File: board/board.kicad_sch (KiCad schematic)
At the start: 8 parts, among them J1 015_RGMII, J2 020_1000BASE-T_with_CT, J3 Conn_01x03_Male

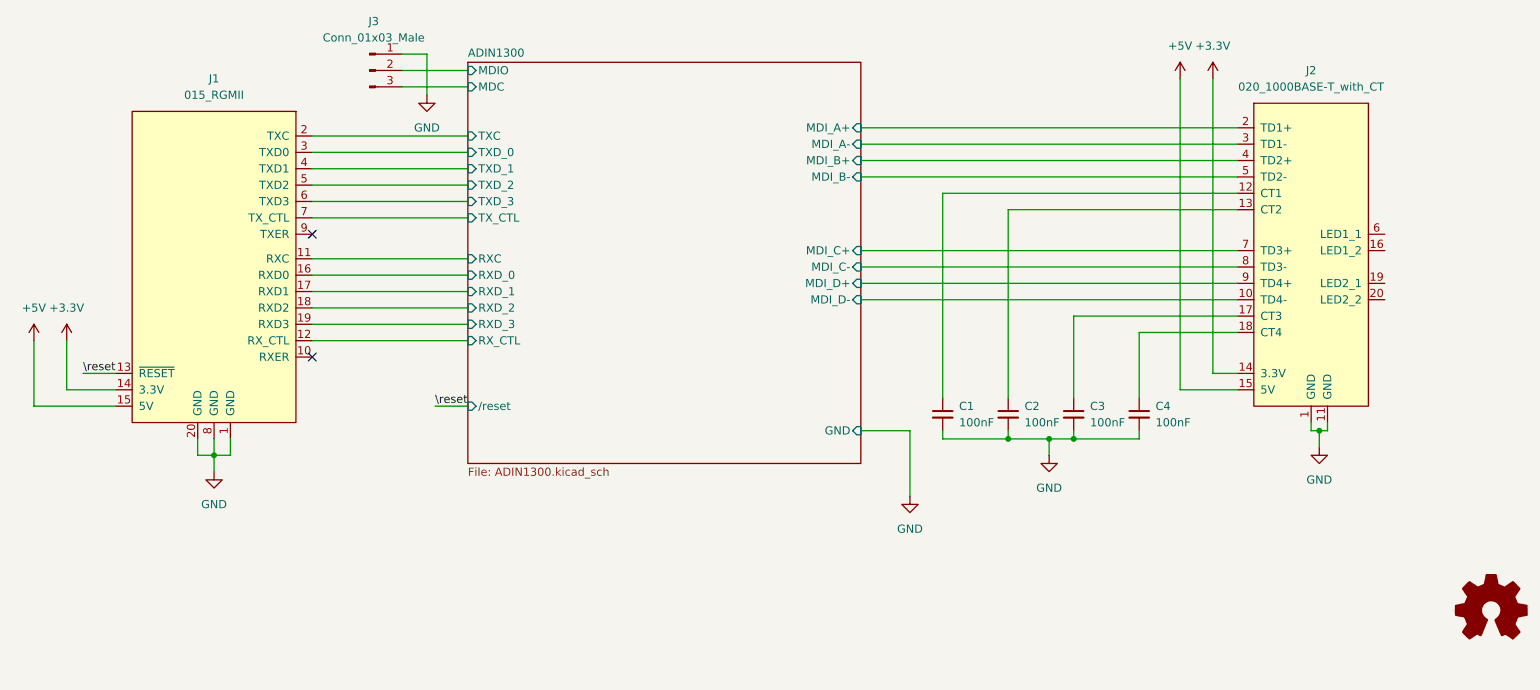
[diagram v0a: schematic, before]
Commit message: optimized EMI
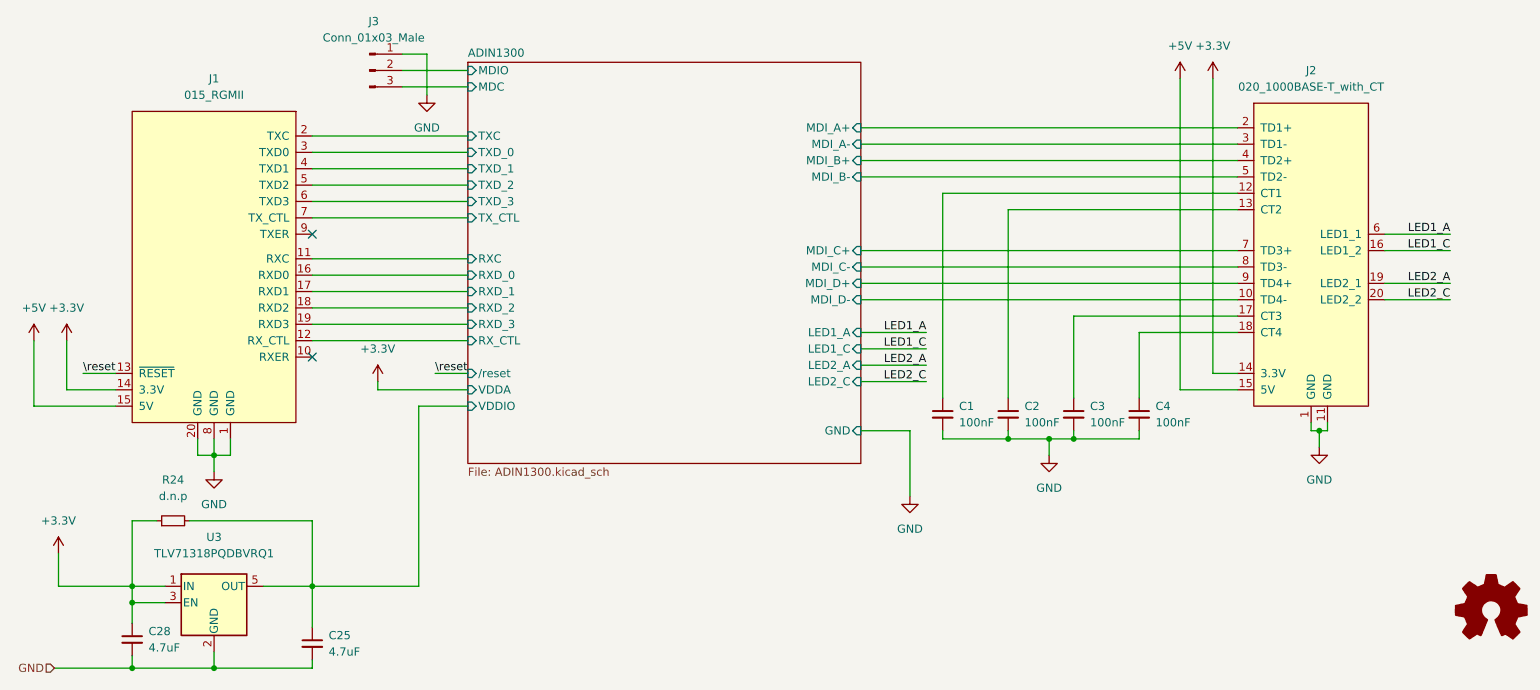
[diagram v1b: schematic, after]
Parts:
- added C25, C28: 4.7uF, Capacitor_SMD:C_0603_1608Metric, symbol Device:C_Small
- added R24: d.n.p, Resistor_SMD:R_0603_1608Metric, symbol Device:R_Small
- added U3: TLV71318PQDBVRQ1, Package_TO_SOT_SMD:SOT-23-5, symbol Regulator_Linear:TLV71209_SOT23-5
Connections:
- net +3.3V: now also C28.1, R24.1, U3.1 (IN), U3.3 (EN)
- net GND: now also C25.2, C28.2, U3.2 (GND)
- net LED1_C: now reaches J2.16 (LED1_2)
- net LED2_A: now reaches J2.19 (LED2_1)
- net LED2_C: now reaches J2.20 (LED2_2)
- net LED1_A: now reaches J2.6 (LED1_1)
- new net ADIN1300/VDDIO: C25.1, R24.2, U3.5 (OUT)
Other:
- sheet ADIN1300 ports: added LED1_A, LED1_C, LED2_A, LED2_C, VDDA, VDDIO; removed none
